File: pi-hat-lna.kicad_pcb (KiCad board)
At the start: 4 copper layers, 65 x 56 mm, 109 parts, among them J1 USB_B_Mini, J3 40HAT, J4 VAL**, J5 VAL**, J6 2x3 0.1" HEADER, J7 VAL**, J8 VAL**, J9 CONN_01X02, M1 2118706-2, M2 2118706-2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

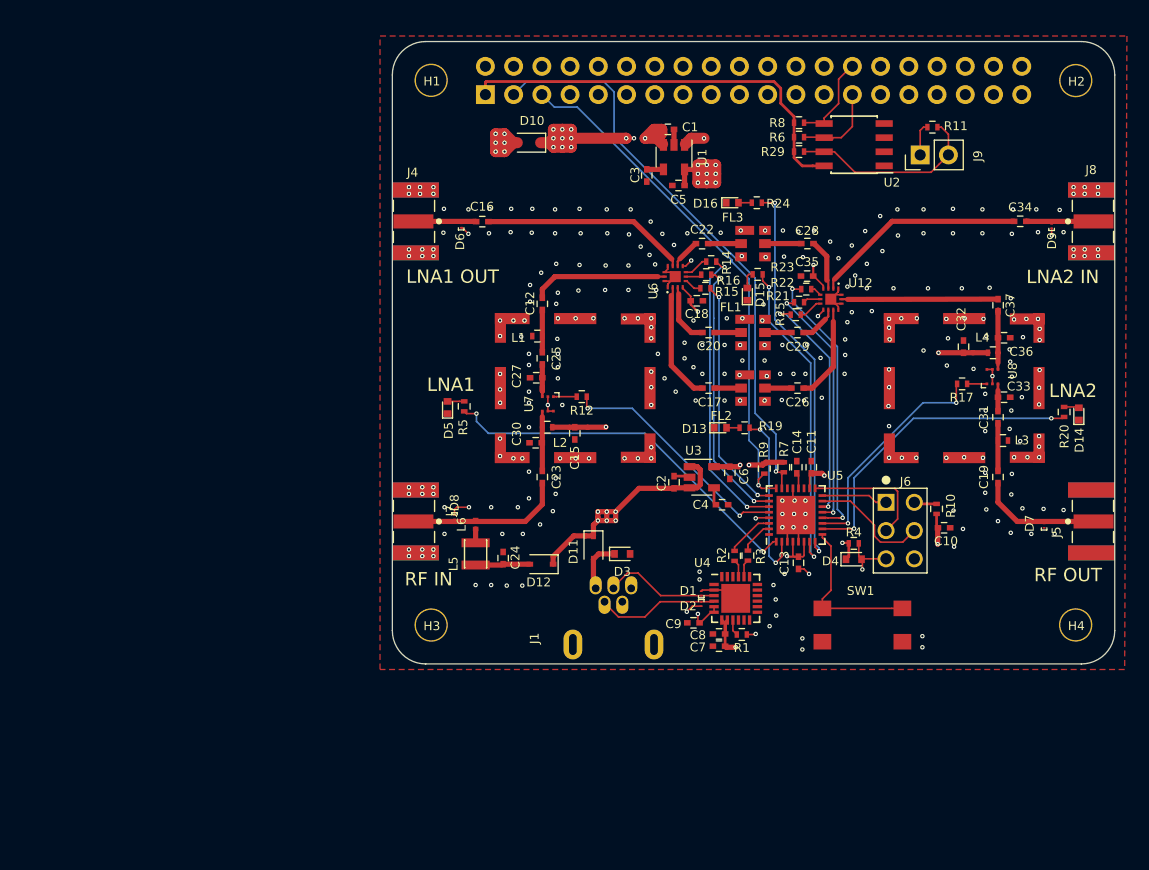
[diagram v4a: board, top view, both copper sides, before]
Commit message: Cleaned up BOM and added part numbers to the layout.
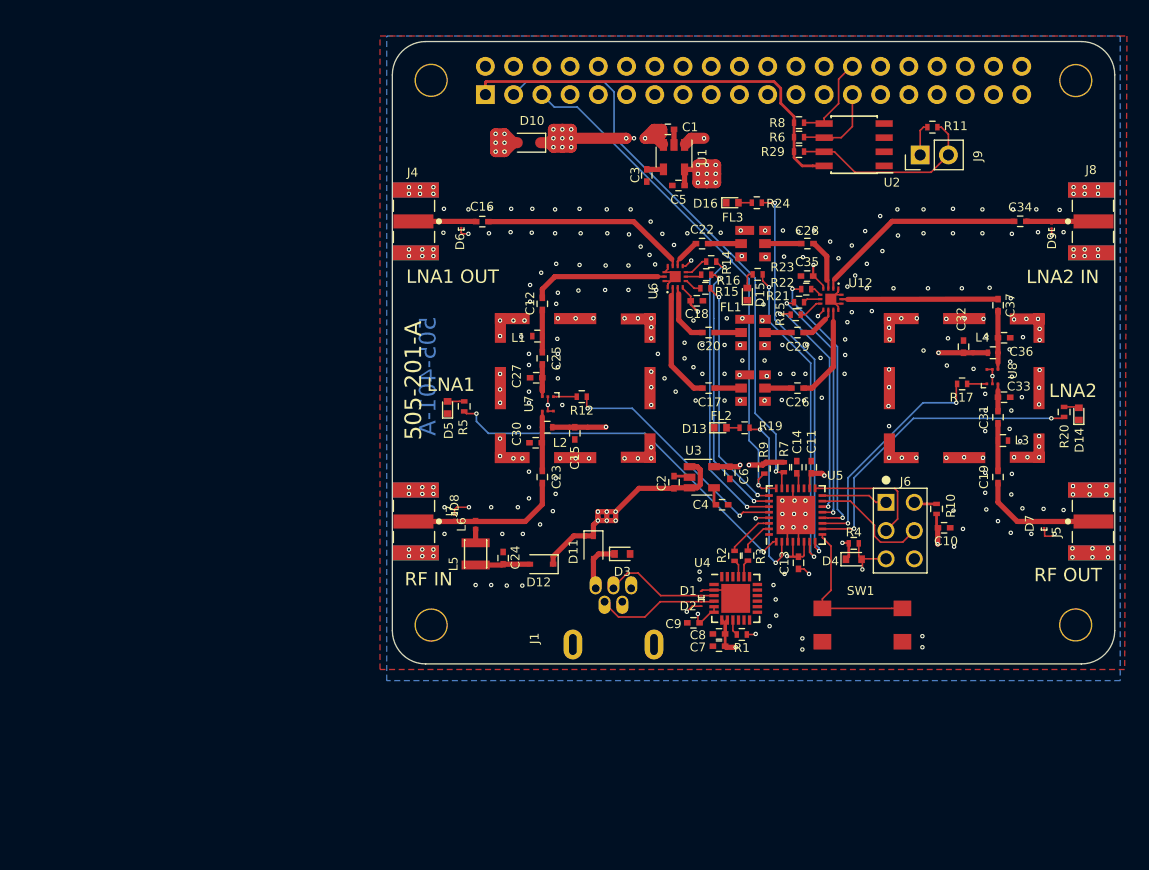
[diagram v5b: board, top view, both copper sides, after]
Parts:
- J3: value 40HAT -> DNF
- J4, J5, J7, J8: value VAL** -> SMA-J-P-H-ST-EM1
- SW1: value VAL** -> TL3305AF160QG
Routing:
- net GND: track 33.8 -> 35.8 mm, vias 299 -> 311
- added copper zone on B.Cu, net GND
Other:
- board text added: "505-201-A"
- board text added: "505-401-A"
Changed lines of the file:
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@@
   (general
     (thickness 1.6)
-    (drawings 85)
-    (tracks 961)
+    (drawings 87)
+    (tracks 979)
     (zones 0)
     (modules 109)
@@
   )
   (setup
-    (last_trace_width 1)
+    (last_trace_width 0.15)
     (user_trace_width 0.15)
     (user_trace_width 0.2)
@@
     (visible_elements 7FFFFE7F)
     (pcbplotparams
-      (layerselection 0x010f8_80000007)
+      (layerselection 0x010e8_ffffffff)
       (usegerberextensions false)
       (usegerberattributes false)
@@
   (module project_footprints:NPTH_3mm_ID locked (layer F.Cu)
     (at 82.04 64.31)
-    (fp_text reference H1 (at 0.06 0.09) (layer F.SilkS)
+    (fp_text reference H1 (at 0.06 0.09) (layer F.SilkS) hide
       (effects (font (size 0.8 0.8) (thickness 0.15)))
     )
@@
   (module project_footprints:NPTH_3mm_ID locked (layer F.Cu)
     (at 140.04 64.33)
-    (fp_text reference H2 (at 0.06 0.09) (layer F.SilkS)
+    (fp_text reference H2 (at 0.06 0.09) (layer F.SilkS) hide
       (effects (font (size 0.8 0.8) (thickness 0.15)))
     )
@@
   (module project_footprints:NPTH_3mm_ID locked (layer F.Cu)
     (at 82.04 113.32)
-    (fp_text reference H3 (at 0.06 0.09) (layer F.SilkS)
+    (fp_text reference H3 (at 0.06 0.09) (layer F.SilkS) hide
       (effects (font (size 0.8 0.8) (thickness 0.15)))
     )
@@
   (module project_footprints:NPTH_3mm_ID locked (layer F.Cu)
     (at 140.03 113.31)
-    (fp_text reference H4 (at 0.06 0.09) (layer F.SilkS)
+    (fp_text reference H4 (at 0.06 0.09) (layer F.SilkS) hide
       (effects (font (size 0.8 0.8) (thickness 0.15)))
     )
@@
     (descr "Through hole straight socket strip, 2x20, 2.54mm pitch, double cols (from Kicad 4.0.7), script generated")
     (tags "Through hole socket strip THT 2x20 2.54mm double row")
-    (fp_text reference J3 (at -1.27 2.77 270) (layer B.SilkS)
+    (fp_text reference J3 (at 2.33 1.88 270) (layer B.SilkS)
       (effects (font (size 0.8 0.8) (thickness 0.15)) (justify mirror))
     )
-    (fp_text value 40HAT (at -1.27 -51.03 270) (layer B.Fab)
+    (fp_text value DNF (at -1.27 -51.03 270) (layer B.Fab)
       (effects (font (size 0.5 0.5) (thickness 0.09)) (justify mirror))
     )
@@
       (effects (font (size 0.8 0.8) (thickness 0.15)))
     )
-    (fp_text value VAL** (at 0.175614 4.88242) (layer F.SilkS) hide
+    (fp_text value TL3305AF160QG (at 0.175614 4.88242) (layer F.SilkS) hide
       (effects (font (size 0.5 0.5) (thickness 0.09)))
     )
@@
       (effects (font (size 0.8 0.8) (thickness 0.15)))
     )
-    (fp_text value VAL** (at -0.225387 12.3855 270) (layer F.SilkS) hide
+    (fp_text value SMA-J-P-H-ST-EM1 (at -0.225387 12.3855 270) (layer F.SilkS) hide
       (effects (font (size 1.00166 1.00166) (thickness 0.05)))
     )
@@
       (effects (font (size 0.8 0.8) (thickness 0.15)))
     )
-    (fp_text value VAL** (at -0.225387 12.3855 90) (layer F.SilkS) hide
+    (fp_text value SMA-J-P-H-ST-EM1 (at -0.225387 12.3855 90) (layer F.SilkS) hide
       (effects (font (size 1.00166 1.00166) (thickness 0.05)))
     )
@@
       (effects (font (size 0.8 0.8) (thickness 0.15)))
     )
-    (fp_text value VAL** (at -0.225387 12.3855 270) (layer F.SilkS) hide
+    (fp_text value SMA-J-P-H-ST-EM1 (at -0.225387 12.3855 270) (layer F.SilkS) hide
       (effects (font (size 1.00166 1.00166) (thickness 0.05)))
     )
@@
       (effects (font (size 0.8 0.8) (thickness 0.15)))
     )
-    (fp_text value VAL** (at 5.78 -4.5 90) (layer F.SilkS) hide
+    (fp_text value SMA-J-P-H-ST-EM1 (at 5.78 -4.5 90) (layer F.SilkS) hide
       (effects (font (size 1.00166 1.00166) (thickness 0.05)))
     )
@@
     )
   )
+  (gr_text 505-401-A (at 81.74 90.92 90) (layer B.Cu)
+    (effects (font (size 1.5 1.5) (thickness 0.3)) (justify mirror))
+  )
+  (gr_text 505-201-A (at 80.44 91.32 90) (layer F.SilkS)
+    (effects (font (size 1.5 1.5) (thickness 0.3)))
+  )
   (gr_text "LNA2 IN" (at 138.865 81.995) (layer F.SilkS)
     (effects (font (size 1.2 1.2) (thickness 0.2)))
@@
   (gr_line (start 81.546356 116.817611) (end 140.546356 116.817611) (layer Edge.Cuts) (width 0.1))
   (gr_arc (start 140.546356 113.817611) (end 140.546356 116.817611) (angle -89.9) (layer Edge.Cuts) (width 0.1))
+  (via (at 139.74 107.22) (size 0.4) (drill 0.2) (layers F.Cu B.Cu) (net 1))
+  (via (at 139.74 106.42) (size 0.4) (drill 0.2) (layers F.Cu B.Cu) (net 1))
+  (via (at 141.54 106.42) (size 0.4) (drill 0.2) (layers F.Cu B.Cu) (net 1))
+  (via (at 141.54 107.22) (size 0.4) (drill 0.2) (layers F.Cu B.Cu) (net 1))
+  (via (at 142.94 107.22) (size 0.4) (drill 0.2) (layers F.Cu B.Cu) (net 1))
+  (via (at 142.94 106.42) (size 0.4) (drill 0.2) (layers F.Cu B.Cu) (net 1))
+  (via (at 139.79 101.57) (size 0.4) (drill 0.2) (layers F.Cu B.Cu) (net 1))
+  (via (at 139.79 100.82) (size 0.4) (drill 0.2) (layers F.Cu B.Cu) (net 1))
+  (via (at 141.29 101.57) (size 0.4) (drill 0.2) (layers F.Cu B.Cu) (net 1))
+  (via (at 141.29 100.82) (size 0.4) (drill 0.2) (layers F.Cu B.Cu) (net 1))
+  (via (at 142.79 101.57) (size 0.4) (drill 0.2) (layers F.Cu B.Cu) (net 1))
+  (via (at 142.79 100.82) (size 0.4) (drill 0.2) (layers F.Cu B.Cu) (net 1))
   (via (at 123.24 90.32) (size 0.4) (drill 0.2) (layers F.Cu B.Cu) (net 1))
   (via (at 123.24 91.92) (size 0.4) (drill 0.2) (layers F.Cu B.Cu) (net 1))
@@
   (via (at 85.39 78.12) (size 0.4) (drill 0.2) (layers F.Cu B.Cu) (net 1))
   (via (at 83.14 78.02) (size 0.4) (drill 0.2) (layers F.Cu B.Cu) (net 1))
-  (segment (start 84.84 77.57) (end 85.39 78.12) (width 0.15) (layer F.Cu) (net 1))
-  (segment (start 84.74 77.57) (end 84.84 77.57) (width 0.15) (layer F.Cu) (net 1))
   (via (at 83.19 75.87) (size 0.4) (drill 0.2) (layers F.Cu B.Cu) (net 1))
   (via (at 85.39 75.92) (size 0.4) (drill 0.2) (layers F.Cu B.Cu) (net 1))
@@
   (via (at 115.714979 104.52) (size 0.4) (drill 0.2) (layers F.Cu B.Cu) (net 1))
   (via (at 117.19 92.87) (size 0.4) (drill 0.2) (layers F.Cu B.Cu) (net 1))
+  (segment (start 84.74 77.57) (end 84.74 78.02) (width 0.15) (layer F.Cu) (net 1))
+  (segment (start 84.84 78.12) (end 85.39 78.12) (width 0.15) (layer F.Cu) (net 1))
+  (segment (start 84.74 78.02) (end 84.84 78.12) (width 0.15) (layer F.Cu) (net 1))
+  (segment (start 137.19 104.795) (end 137.24 104.845) (width 0.15) (layer F.Cu) (net 1))
+  (segment (start 137.19 104.57) (end 137.19 104.795) (width 0.15) (layer F.Cu) (net 1))
+  (segment (start 137.24 104.845) (end 137.24 105.32) (width 0.15) (layer F.Cu) (net 1))
+  (segment (start 137.940001 105.319999) (end 138.14 105.12) (width 0.15) (layer F.Cu) (net 1))
+  (segment (start 137.24 105.32) (end 137.940001 105.319999) (width 0.15) (layer F.Cu) (net 1))
   (segment (start 119.94 65.59) (end 119.94 68.46) (width 0.15) (layer F.Cu) (net 2))
   (segment (start 118.935 69.465) (end 117.4 69.465) (width 0.15) (layer F.Cu) (net 2))
@@
   (segment (start 107.49 102.32) (end 107.665 102.495) (width 0.25) (layer F.Cu) (net 8))
   (segment (start 107.49 100.97) (end 107.49 102.32) (width 0.25) (layer F.Cu) (net 8))
-  (segment (start 117.4 72.005) (end 116.695 72.005) (width 0.15) (layer F.Cu) (net 83))
-  (segment (start 80.57 103.87) (end 80.44 104) (width 0.47) (layer F.Cu) (net 23))
   (segment (start 92.94 95.52) (end 94.49 95.52) (width 0.47) (layer F.Cu) (net 9))
   (segment (start 132.14 88.82) (end 130.79 88.82) (width 0.47) (layer F.Cu) (net 9))
@@
   (segment (start 105.865 79) (end 105.815 79) (width 0.47) (layer F.Cu) (net 21))
   (segment (start 106.965 79) (end 109.925 79) (width 0.47) (layer F.Cu) (net 22))
+  (segment (start 80.57 103.87) (end 80.44 104) (width 0.47) (layer F.Cu) (net 23))
   (segment (start 80.44 104) (end 90.51 104) (width 0.47) (layer F.Cu) (net 23))
   (segment (start 92.04 102.47) (end 92.04 100.55) (width 0.47) (layer F.Cu) (net 23))
@@
   (segment (start 118.9525 84) (end 119.35 84) (width 0.2) (layer F.Cu) (net 82))
   (segment (start 133.05 83.995) (end 119.515 84.02) (width 0.47) (layer F.Cu) (net 82))
+  (segment (start 117.4 72.005) (end 116.695 72.005) (width 0.15) (layer F.Cu) (net 83))
   (segment (start 113.495001 66.375001) (end 114.69 67.57) (width 0.25) (layer F.Cu) (net 83))
   (segment (start 113.495001 65.025999) (end 113.495001 66.375001) (width 0.25) (layer F.Cu) (net 83))
@@
       )
     )
+  )
+  (zone (net 1) (net_name GND) (layer B.Cu) (hatch edge 0.508)
+    (connect_pads yes (clearance 0.4))
+    (min_thickness 0.254)
+    (fill yes (arc_segments 16) (thermal_gap 0.508) (thermal_bridge_width 0.508))
+    (polygon
+      (pts
+        (xy 78.04 60.32) (xy 144.04 60.32) (xy 144.04 118.32) (xy 78.04 118.32)
+      )
+    )

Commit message: Cleaned up all vias and tracks. FYI - always work in mils!!!
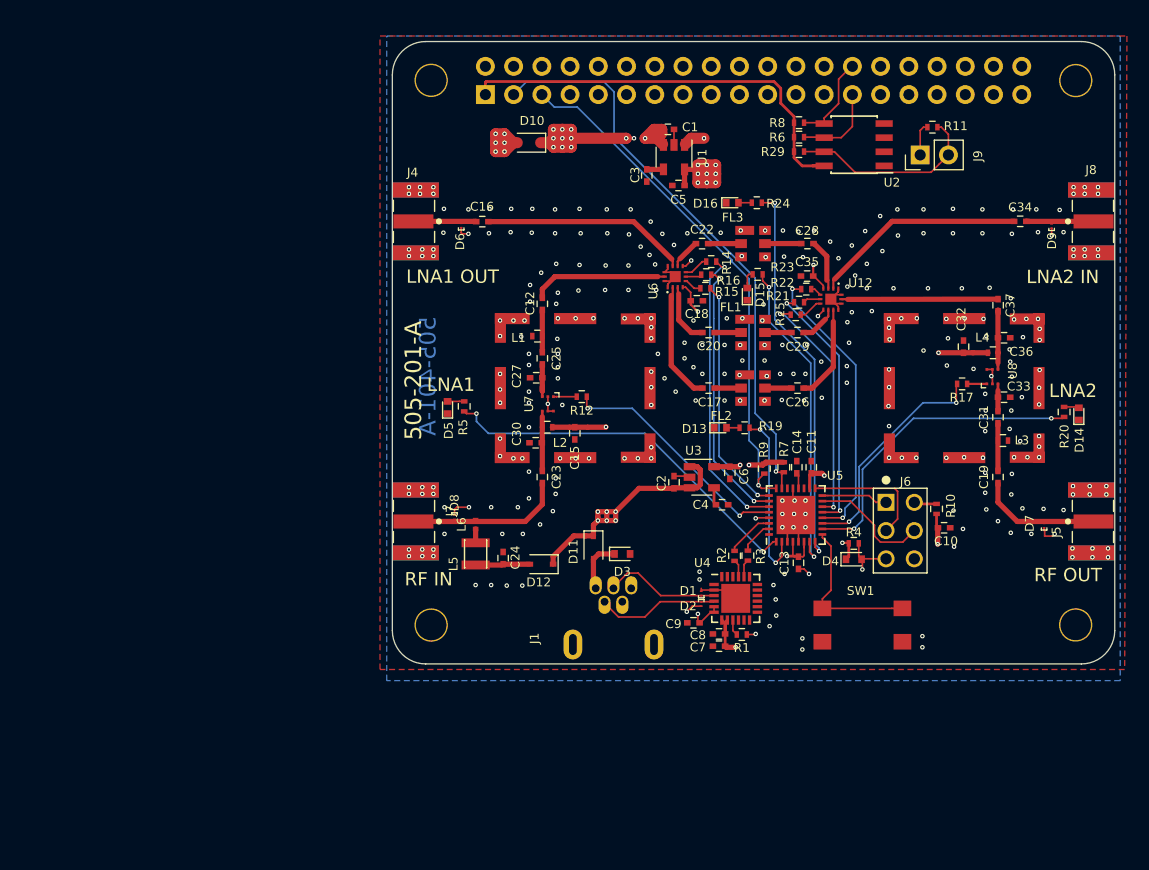
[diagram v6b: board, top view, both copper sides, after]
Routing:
- net /avr-usb/SWB_V3: track 25.1 -> 26.1 mm
- net /avr-usb/SWB_V2: track 22.3 -> 23.0 mm
- net /avr-usb/SWB_V1: track 21.1 -> 21.7 mm
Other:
- net class Default: trace_width 0.15 -> 0.1524; via_dia 0.4 -> 0.4064; via_drill 0.2 -> 0.2032
- rule trace_min: 0.15 -> 0.1524
- rule via_min_drill: 0.2 -> 0.2032
- rule via_min_size: 0.4 -> 0.4064

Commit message: Board is out for quote to several places.
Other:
- board text added: "1oz or 0.5oz"
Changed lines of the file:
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@@
   )
   (page A4)
+  (title_block
+    (title 505-201)
+    (rev A)
+    (company bobbyjsmith11@gmail.com)
+  )
   (layers
     (0 F.Cu signal)
@@
     (visible_elements 7FFFFE7F)
     (pcbplotparams
-      (layerselection 0x010e8_ffffffff)
+      (layerselection 0x010f8_ffffffff)
       (usegerberextensions false)
       (usegerberattributes false)
@@
     (effects (font (size 1.2 1.2) (thickness 0.2)))
   )
-  (gr_text "50 Ohm trace = 18.5 mil (0.47 mm)" (at 195.54 92.32) (layer Dwgs.User)
+  (gr_text "50 Ohm trace = 18.5 mil (0.47 mm)" (at 195.54 92.32) (layer Cmts.User)
     (effects (font (size 1.5 1.5) (thickness 0.3)))
   )
-  (gr_text "9.3 mil ?" (at 215.54 83.32) (layer Dwgs.User)
+  (gr_text "9.3 mil ?" (at 215.54 83.32) (layer Cmts.User)
     (effects (font (size 1.5 1.5) (thickness 0.3)))
   )
-  (gr_text "9.3 mil ?" (at 215.29 73.07) (layer Dwgs.User)
+  (gr_text "9.3 mil ?" (at 215.29 73.07) (layer Cmts.User)
     (effects (font (size 1.5 1.5) (thickness 0.3)))
   )
-  (gr_line (start 226.79 85.07) (end 226.79 80.82) (layer Dwgs.User) (width 0.15))
-  (gr_line (start 226.79 75.82) (end 226.79 71.57) (layer Dwgs.User) (width 0.15))
-  (gr_text 0.062" (at 227.29 78.32) (layer Dwgs.User)
+  (gr_line (start 226.79 85.07) (end 226.79 80.82) (layer Cmts.User) (width 0.15))
+  (gr_line (start 226.79 75.82) (end 226.79 71.57) (layer Cmts.User) (width 0.15))
+  (gr_text 0.062" (at 227.29 78.32) (layer Cmts.User)
     (effects (font (size 1.5 1.5) (thickness 0.3)))
   )
-  (gr_line (start 224.29 85.82) (end 229.29 85.82) (layer Dwgs.User) (width 0.15))
-  (gr_line (start 224.29 70.82) (end 229.29 70.82) (layer Dwgs.User) (width 0.15))
-  (gr_text "2116 Prepreg (x2)" (at 197.29 83.32) (layer Dwgs.User)
+  (gr_line (start 224.29 85.82) (end 229.29 85.82) (layer Cmts.User) (width 0.15))
+  (gr_line (start 224.29 70.82) (end 229.29 70.82) (layer Cmts.User) (width 0.15))
+  (gr_text "2116 Prepreg (x2)" (at 197.29 83.32) (layer Cmts.User)
     (effects (font (size 1.5 1.5) (thickness 0.3)))
   )
-  (gr_text "2116 Prepreg (x2)" (at 197.04 73.07) (layer Dwgs.User)
+  (gr_text "2116 Prepreg (x2)" (at 197.04 73.07) (layer Cmts.User)
     (effects (font (size 1.5 1.5) (thickness 0.3)))
   )
-  (gr_text "0.039\" FR4 core" (at 205.04 78.57) (layer Dwgs.User)
+  (gr_text "0.039\" FR4 core" (at 205.04 78.57) (layer Cmts.User)
     (effects (font (size 1.5 1.5) (thickness 0.3)))
   )
-  (gr_text "1 oz Cu" (at 179.29 85.57) (layer Dwgs.User)
+  (gr_text "1 oz Cu" (at 179.29 85.57) (layer Cmts.User)
     (effects (font (size 1.5 1.5) (thickness 0.3)))
   )
-  (gr_text "1 oz Cu" (at 179.29 80.57) (layer Dwgs.User)
+  (gr_text "1oz or 0.5oz" (at 176.84 81.02) (layer Cmts.User)
     (effects (font (size 1.5 1.5) (thickness 0.3)))
   )
-  (gr_text "1 oz Cu" (at 179.29 75.32) (layer Dwgs.User)
+  (gr_text "1oz or 0.5oz" (at 176.64 75.22) (layer Cmts.User)
     (effects (font (size 1.5 1.5) (thickness 0.3)))
   )
-  (gr_text "1 oz Cu" (at 179.29 70.82) (layer Dwgs.User)
+  (gr_text "1 oz Cu" (at 179.29 70.82) (layer Cmts.User)
     (effects (font (size 1.5 1.5) (thickness 0.3)))
   )
-  (gr_line (start 222.04 70.82) (end 222.04 85.82) (layer Dwgs.User) (width 0.15))
-  (gr_line (start 184.54 70.82) (end 184.54 85.82) (layer Dwgs.User) (width 0.15))
-  (gr_line (start 184.54 85.82) (end 222.04 85.82) (layer Dwgs.User) (width 0.15))
-  (gr_line (start 184.54 81.82) (end 222.04 81.82) (layer Dwgs.User) (width 0.15))
-  (gr_line (start 184.54 75.57) (end 222.04 75.57) (layer Dwgs.User) (width 0.15))
-  (gr_line (start 184.54 70.82) (end 222.04 70.82) (layer Dwgs.User) (width 0.15))
-  (gr_line (start 184.54 85.07) (end 222.04 85.07) (layer Dwgs.User) (width 0.15))
-  (gr_line (start 184.54 81.07) (end 222.04 81.07) (layer Dwgs.User) (width 0.15))
-  (gr_line (start 184.54 74.82) (end 222.04 74.82) (layer Dwgs.User) (width 0.15))
-  (gr_line (start 184.54 71.57) (end 222.04 71.57) (layer Dwgs.User) (width 0.15))
-  (dimension 56 (width 0.3) (layer Dwgs.User)
-    (gr_text "2.2047 in" (at 63.84 88.82 270) (layer Dwgs.User)
+  (gr_line (start 222.04 70.82) (end 222.04 85.82) (layer Cmts.User) (width 0.15))
+  (gr_line (start 184.54 70.82) (end 184.54 85.82) (layer Cmts.User) (width 0.15))
+  (gr_line (start 184.54 85.82) (end 222.04 85.82) (layer Cmts.User) (width 0.15))
+  (gr_line (start 184.54 81.82) (end 222.04 81.82) (layer Cmts.User) (width 0.15))
+  (gr_line (start 184.54 75.57) (end 222.04 75.57) (layer Cmts.User) (width 0.15))
+  (gr_line (start 184.54 70.82) (end 222.04 70.82) (layer Cmts.User) (width 0.15))
+  (gr_line (start 184.54 85.07) (end 222.04 85.07) (layer Cmts.User) (width 0.15))
+  (gr_line (start 184.54 81.07) (end 222.04 81.07) (layer Cmts.User) (width 0.15))
+  (gr_line (start 184.54 74.82) (end 222.04 74.82) (layer Cmts.User) (width 0.15))
+  (gr_line (start 184.54 71.57) (end 222.04 71.57) (layer Cmts.User) (width 0.15))
+  (dimension 56 (width 0.3) (layer Cmts.User)
+    (gr_text "2.205 in" (at 63.84 88.82 270) (layer Cmts.User)
       (effects (font (size 1.5 1.5) (thickness 0.3)))
     )
@@
     (arrow2b (pts (xy 65.94 60.82) (xy 66.526421 61.946504)))
   )
-  (dimension 65 (width 0.3) (layer Dwgs.User)
-    (gr_text "2.5591 in" (at 111.04 31.22) (layer Dwgs.User)
+  (dimension 65 (width 0.3) (layer Cmts.User)
+    (gr_text "2.56 in" (at 111.04 31.22) (layer Cmts.User)
       (effects (font (size 1.5 1.5) (thickness 0.3)))
     )
